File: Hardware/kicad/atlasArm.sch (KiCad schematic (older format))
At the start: 10 parts

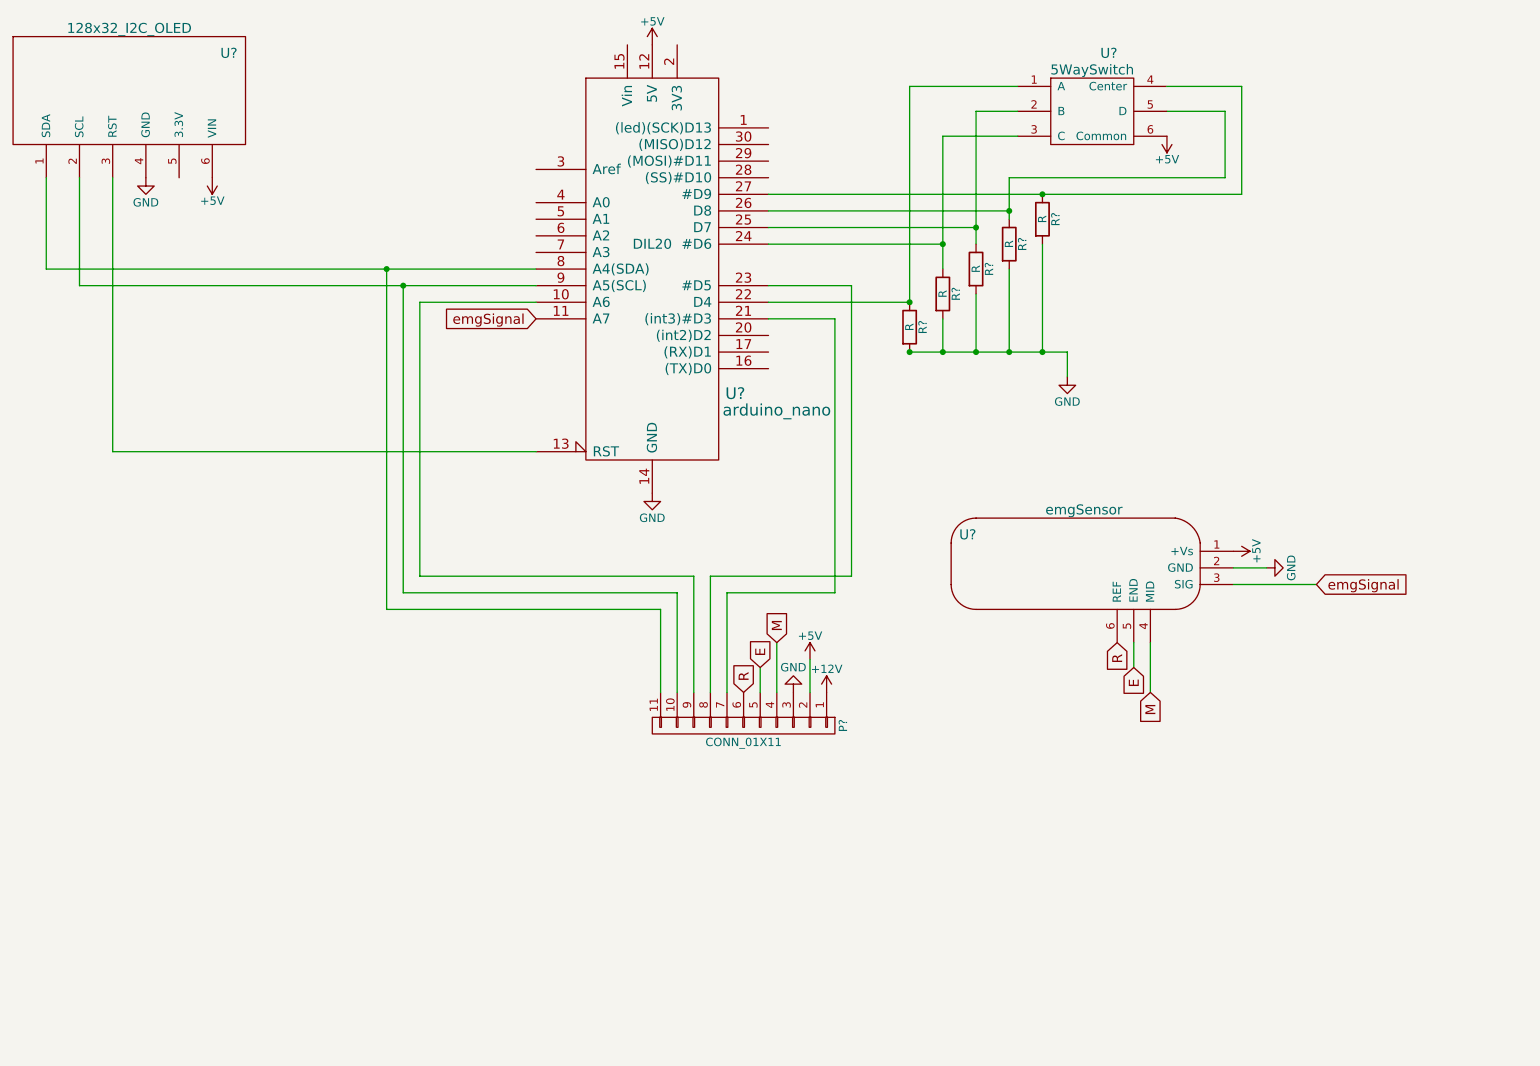
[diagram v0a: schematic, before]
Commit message: added todo text file, added pdf of schematic V5.01
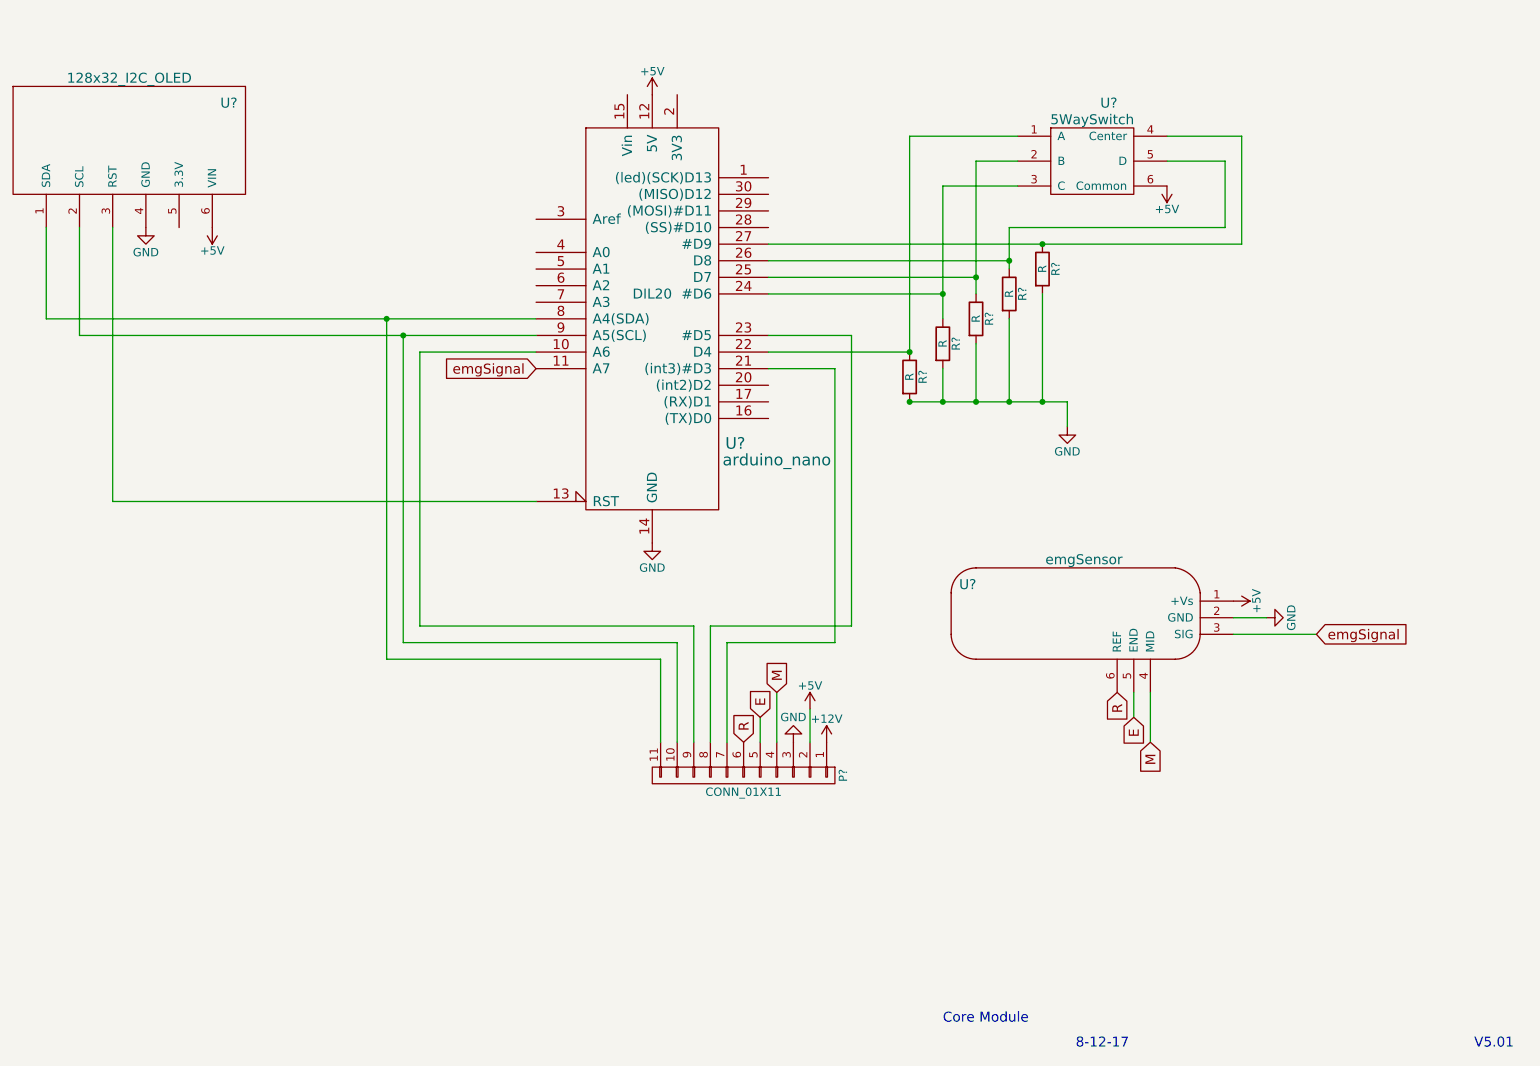
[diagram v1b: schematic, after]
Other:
- note added: "8-12-17"
- note added: "Core Module"
- note added: "V5.01"
- moved on the sheet: P?, R?, U?
